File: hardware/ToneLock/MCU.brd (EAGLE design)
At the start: 160 x 100 mm, 13 parts, among them U1 LD1117S33TR, U2 MP45DT02, U3 LIS3DSHTR

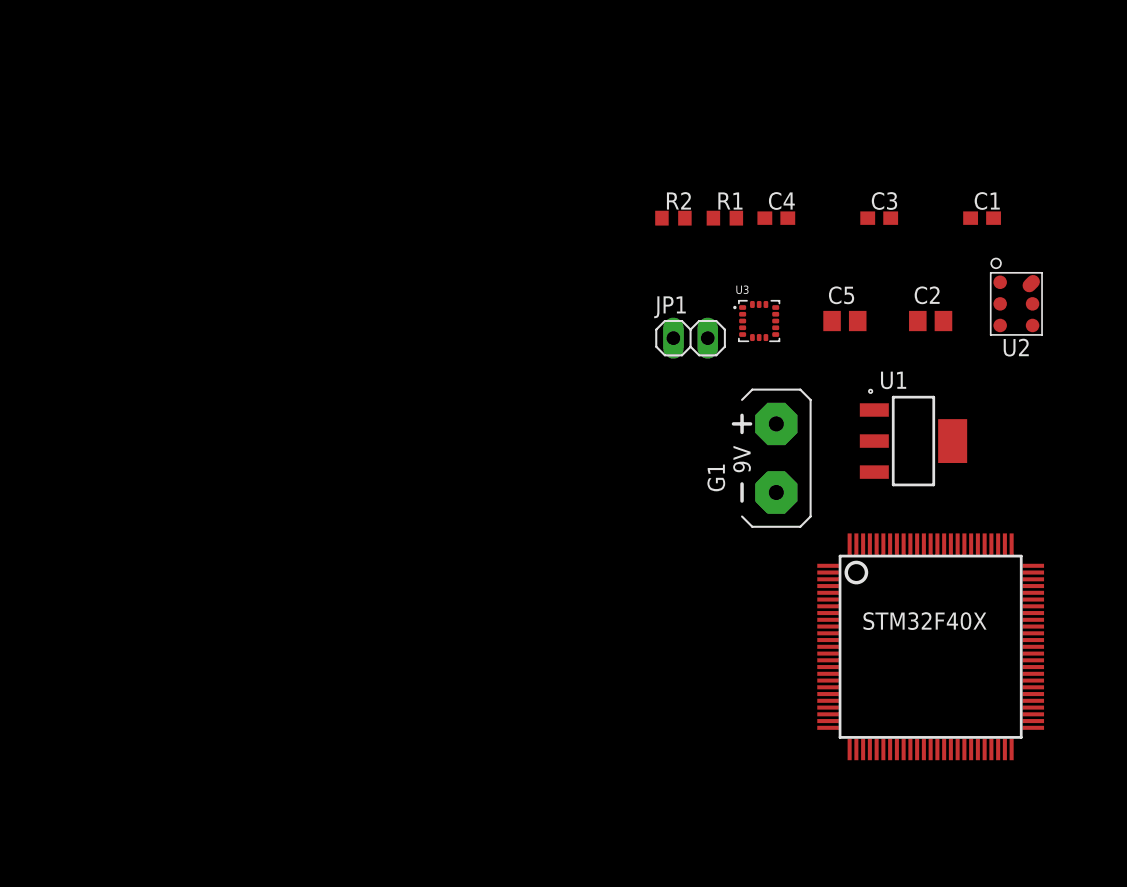
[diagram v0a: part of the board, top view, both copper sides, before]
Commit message: Changed VCC header
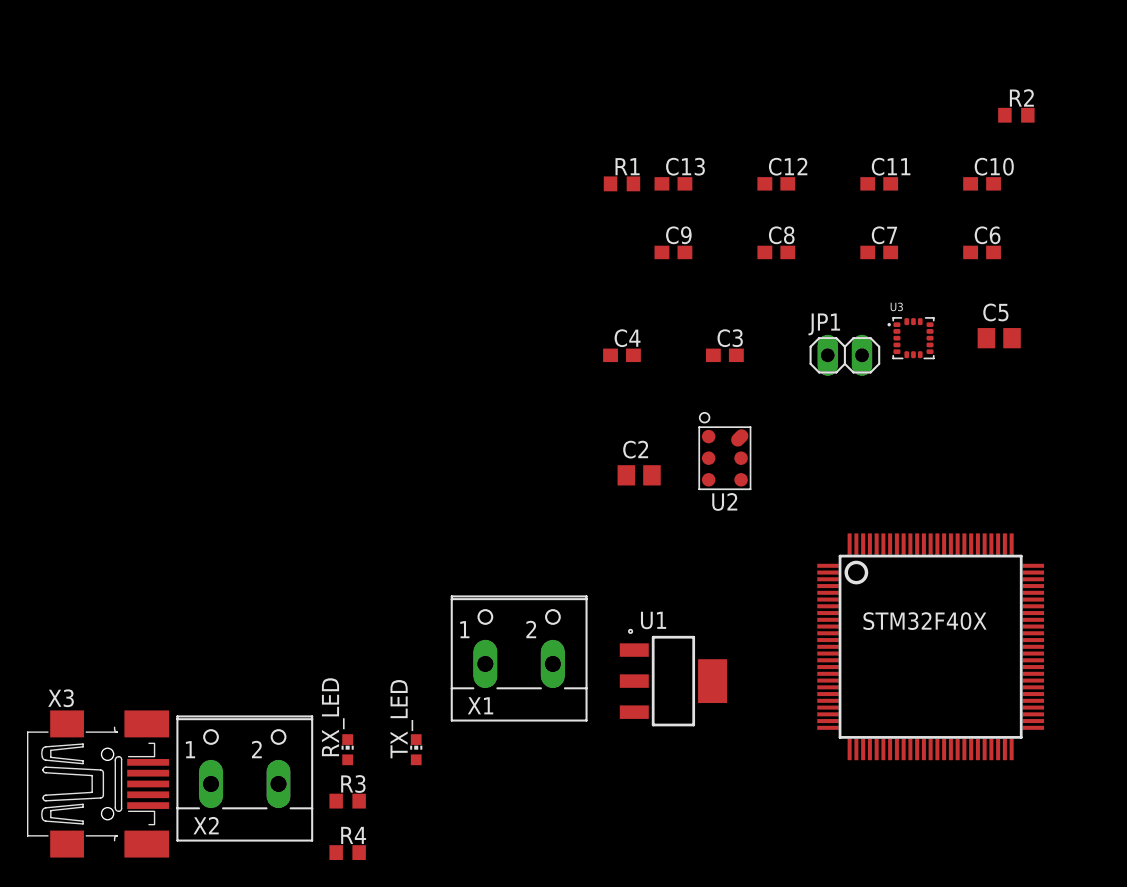
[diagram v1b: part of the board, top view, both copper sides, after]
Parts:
- removed C1: 100nF, resistor:C0603
- removed G1: AB9V, battery:AB9V
- added C10, C11, C12, C13, C6, C7, C8, C9: 100nF, resistor:C0603
- added R3, R4: 330, resistor:R0603
- added RX_LED, TX_LED: (no value), led:CHIP-LED0603
- added X1, X2: (no value), con-wago-500:W237-102
- added X3: MINI-USB-32005-201, con-cypressindustries:32005-201
- moved R2 26.5 mm to (-15.2, 48.3)
- moved U1 25.1 mm to (-40.6, 6.35)
- moved C2 24.4 mm to (-43.2, 21.6)
- moved U2 24.4 mm to (-36.8, 22.9)
- moved C3 15.3 mm to (-36.8, 30.5)
- moved C4 15.3 mm to (-44.5, 30.5)
- moved C5 11.5 mm to (-16.5, 31.8)
- moved U3 11.5 mm to (-22.9, 31.8)
- moved JP1 11.5 mm to (-27.9, 30.5)
- moved R1 8.03 mm to (-44.5, 43.2)
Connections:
- removed net N$2: G1.+, U1.3
- new net N$4: R4.1, RX_LED.C
- new net VCC: U1.3, X1.2
- net GND: now also C10.2, C11.2, C12.2, C13.2, C6.2, C7.2, C8.2, C9.2, U$1.10, U$1.20, U$1.27, U$1.74, U$1.99, X1.1; no longer C1.1, G1.-, U3.13, U3.15, U3.16
- net N$1: now also R3.1, TX_LED.C; no longer C1.2, U$1.11, U$1.6
- net USART2_RX: now also R4.2
- net USART2_TX: now also R3.2
- net VDD: now also C10.1, C11.1, C12.1, C13.1, C6.1, C7.1, C8.1, C9.1, RX_LED.A, TX_LED.A, U$1.100, U$1.11, U$1.19, U$1.21, U$1.22, U$1.28, U$1.50, U$1.6, U$1.75

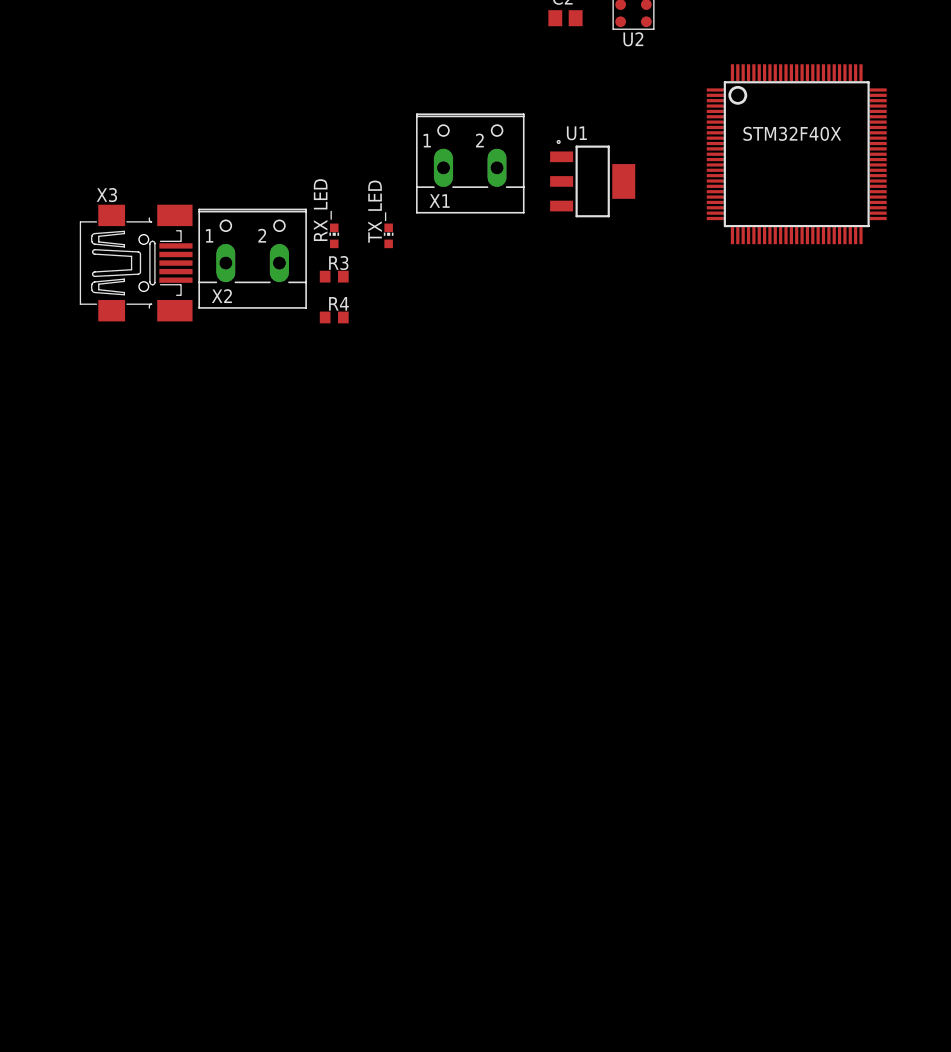
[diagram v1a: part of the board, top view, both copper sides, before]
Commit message: Added BOOT0 and NRST setups, power LED, Debugger
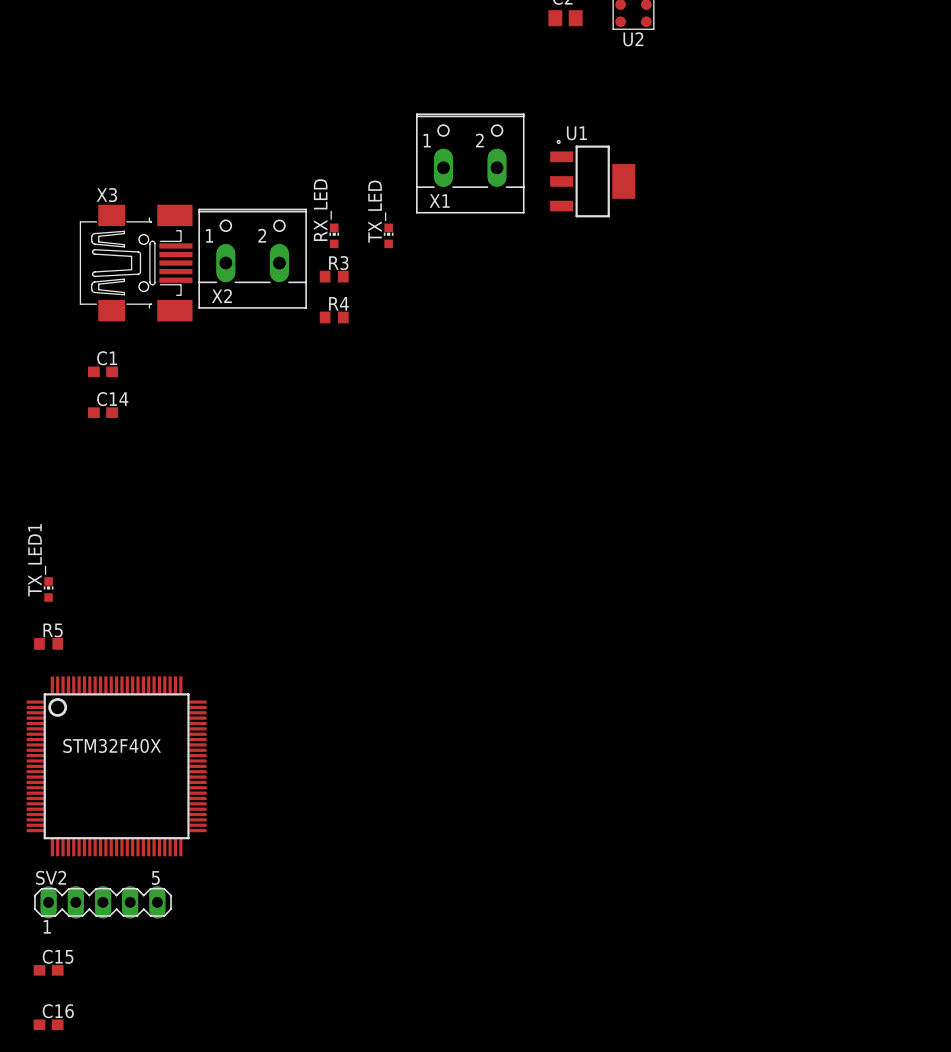
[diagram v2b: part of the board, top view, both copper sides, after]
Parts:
- added C1, C14: 2.2uF, resistor:C0603
- added C15, C16: 10uF, resistor:C0603
- added R5: 330, resistor:R0603
- added SV2: (no value), con-lstb:MA05-1
- added TX_LED1: (no value), led:CHIP-LED0603
- U$1: value STM32F40XSTM32D40X -> STM32F407STM32D40X
- moved U$1 85.4 mm to (-85.1, -48.3)
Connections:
- removed net VCC: U1.3, X1.2
- new net +12V: X1.2
- new net +5V: X3.1
- new net N$2: C14.1, U$1.73
- new net N$5: C1.1, U$1.49
- new net N$6: U1.3
- new net N$7: R5.1, TX_LED1.C
- new net NRST: SV2.5, U$1.14
- new net SWCLK: SV2.2, U$1.76
- new net SWDIO: SV2.4, U$1.72
- net GND: now also C1.2, C14.2, C15.2, C16.2, R5.2, SV2.3, U$1.94, X2.2, X3.5
- net VDD: now also C15.1, C16.1, SV2.1, TX_LED1.A

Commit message: Completed schematic
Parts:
- added D1, D2: BAT54C, diode:SOT23
- added DBG_LED1, DBG_LED2, DBG_LED3, DBG_LED4: (no value), led:CHIP-LED0603
- added Q1: IRLML6346, bss138_10:SOT23
- added R11, R6, R7, R8: 330, resistor:R0603
- added R9: 10k, resistor:R0603
- moved R2 238.6 mm to (-119.4, -166.4)
- moved R1 217.8 mm to (-119.4, -161.3)
- moved R4 140.6 mm to (-119.4, -135.9)
- moved R3 139.4 mm to (-119.4, -130.8)
- moved R5 107.8 mm to (-119.4, -141.0)
- renumbered TX_LED1 to POWER_LED
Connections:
- new net DBG_LED1: DBG_LED1.A, U$1.59
- new net DBG_LED2: DBG_LED2.A, U$1.60
- new net DBG_LED3: DBG_LED3.A, U$1.61
- new net DBG_LED4: DBG_LED4.A, U$1.62
- new net MOSFET_GATE: Q1.1, R9.2, U$1.1
- new net N$10: DBG_LED3.C, R6.1
- new net N$11: DBG_LED2.C, R7.1
- new net N$12: DBG_LED1.C, R8.1
- new net N$8: D2.3, Q1.2, X2.1
- new net N$9: DBG_LED4.C, R5.1
- net +12V: now also D1.2, Q1.3
- net +5V: now also D1.1
- net GND: now also D2.1, D2.2, R1.1, R11.2, R6.2, R7.2, R8.2, R9.1; no longer R2.1
- net N$1: now also POWER_LED.C, R11.1; no longer R3.1, TX_LED.C
- net N$3: now also R1.2, R2.1; no longer R1.1, R2.2
- net N$4: now also R3.1; no longer R4.1
- net N$6: now also D1.3
- net N$7: now also R4.1, TX_LED.C; no longer POWER_LED.C, R5.1
- net USART2_RX: now also R3.2; no longer R4.2
- net USART2_TX: now also R4.2; no longer R3.2
- net VDD: now also R2.2; no longer R1.2

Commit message: Fixed MOSFET switch, grouped all components
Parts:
- added C17: 100nF, resistor:C0603
- moved R2 205.1 mm to (-40.5, 23.0), turned to 90 degrees
- moved R1 196.8 mm to (-40.5, 19.0), turned to 90 degrees
- moved R8 157.0 mm to (-26.0, -30.0), turned to 180 degrees
- moved R7 155.3 mm to (-26.0, -27.0), turned to 180 degrees
- moved R6 153.7 mm to (-26.0, -24.0), turned to 180 degrees
- moved R5 152.0 mm to (-26.0, -21.0), turned to 180 degrees
- moved Q1 135.1 mm to (-108.0, -37.5), turned to 90 degrees
- moved R9 134.7 mm to (-105.0, -37.5), turned to 270 degrees
- moved DBG_LED4 115.7 mm to (-23.0, -21.0), turned to 90 degrees
- moved DBG_LED3 109.9 mm to (-23.0, -24.0), turned to 90 degrees
- moved R4 109.0 mm to (-68.5, -39.5), turned to 270 degrees
- moved DBG_LED2 104.0 mm to (-23.0, -27.0), turned to 90 degrees
- moved U3 103.5 mm to (-35.0, -71.0)
- moved R3 102.4 mm to (-73.0, -39.5), turned to 270 degrees
- moved C4 100.0 mm to (-30.5, -68.5)
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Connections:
- removed net N$8: D2.3, Q1.2, X2.1
- new net N$13: D2.2, Q1.3, X2.2
- net +12V: now also D2.3, X2.1; no longer Q1.3
- net GND: now also C17.2, Q1.2; no longer D2.2, X2.2
- net VDD: now also C17.1
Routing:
- net N$3: track 0.00 -> 6.75 mm
- net N$9: track 0.00 -> 1.40 mm
- net N$12: track 0.00 -> 1.40 mm
- net N$11: track 0.00 -> 1.40 mm
- net N$10: track 0.00 -> 1.40 mm
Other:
- board size 160 x 100 mm -> 71 x 56.5 mm

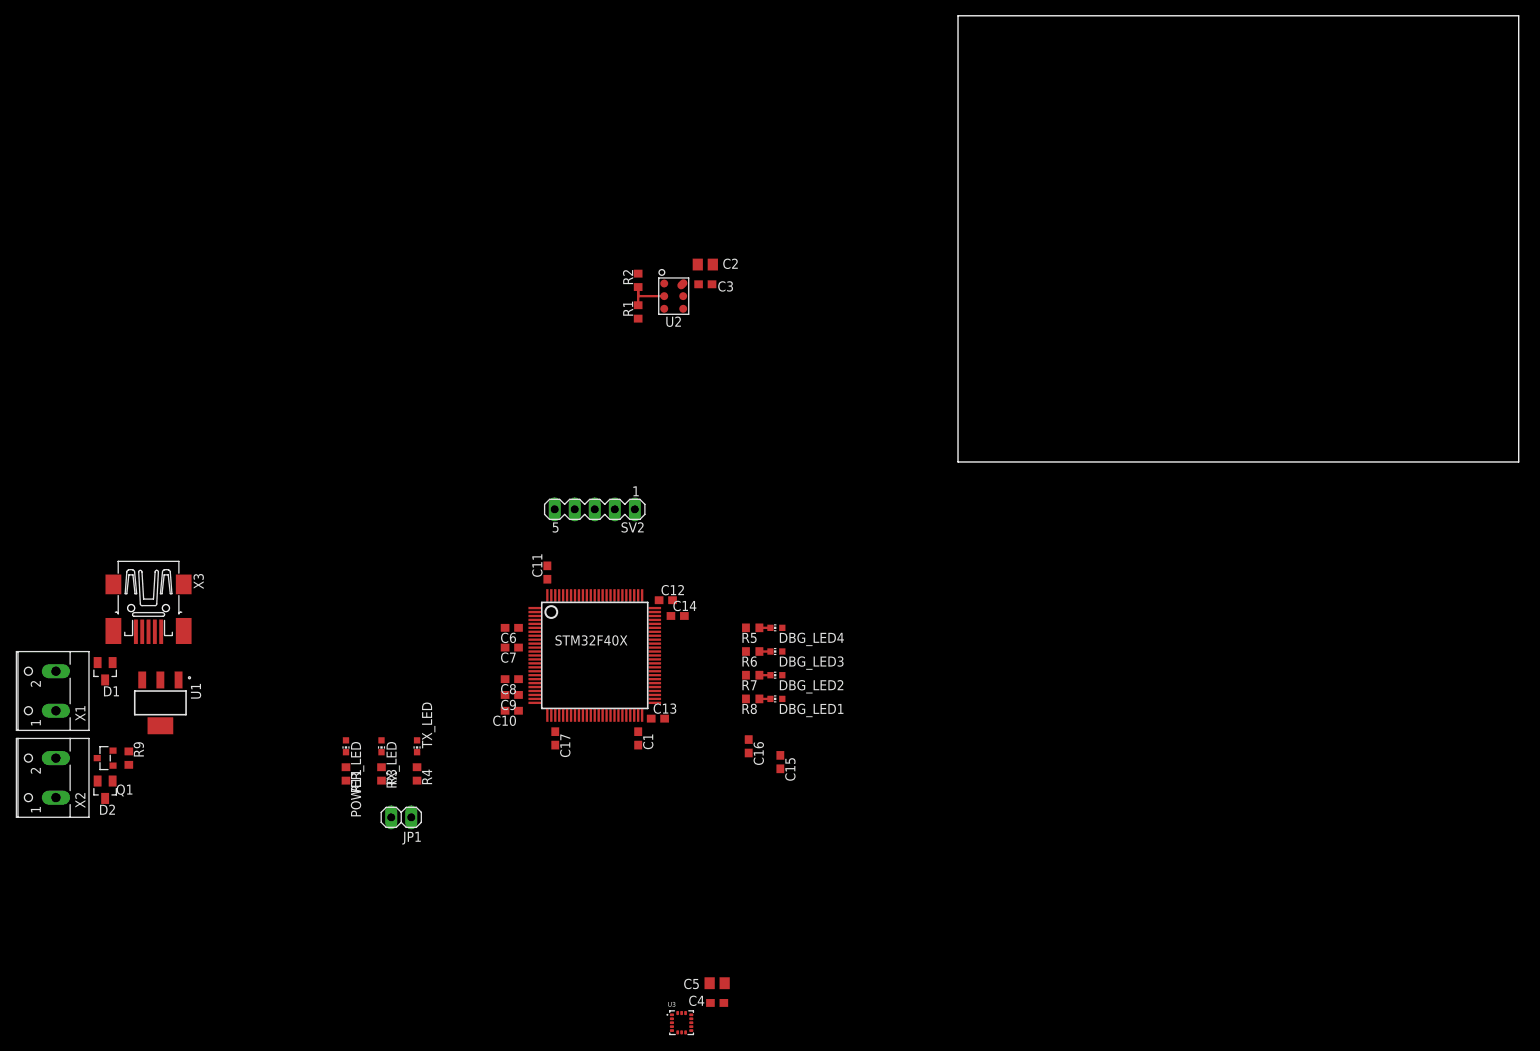
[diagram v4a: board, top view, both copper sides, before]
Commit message: All VCC and signals routed, GND TODO
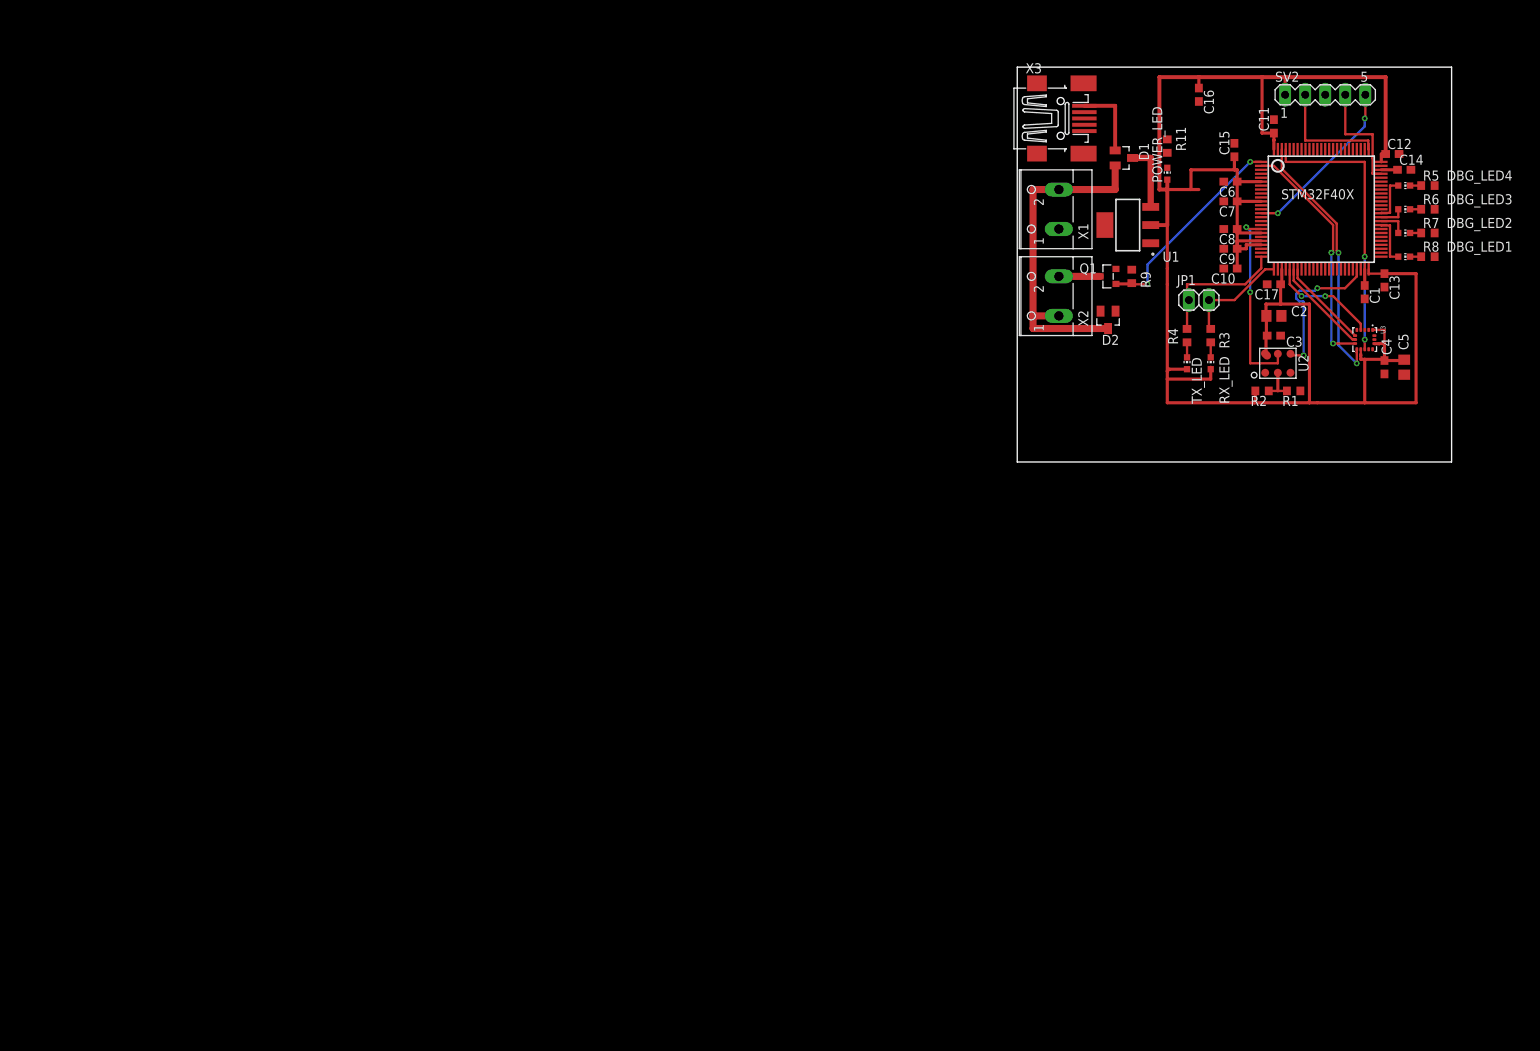
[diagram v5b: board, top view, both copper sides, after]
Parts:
- moved D1 144.5 mm to (21.0, 38.5), turned to 270 degrees
- moved Q1 140.9 mm to (19.0, 23.5)
- moved R9 140.9 mm to (22.0, 23.5)
- moved X1 140.9 mm to (11.5, 32.0)
- moved X2 140.9 mm to (11.5, 21.0)
- moved D2 140.2 mm to (19.0, 18.0)
- moved U1 136.6 mm to (21.5, 30.0), turned to 180 degrees
- moved X3 131.1 mm to (13.0, 43.5), turned to 0 degrees
- moved R11 130.9 mm to (26.5, 40.0), turned to 90 degrees
- moved POWER_LED 126.8 mm to (26.5, 36.5), turned to 0 degrees
- moved U3 122.3 mm to (51.5, 15.5), turned to 270 degrees
- moved JP1 120.4 mm to (30.5, 20.5)
- moved R3 118.8 mm to (32.0, 16.0), turned to 90 degrees
- moved C5 116.8 mm to (56.5, 12.0), turned to 270 degrees
- moved C4 116.7 mm to (54.0, 12.0), turned to 270 degrees
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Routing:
- net VDD: track 0.20 -> 257.6 mm
- net +12V: track 0.10 -> 43.8 mm
- net MEMS_INT1: track 0.00 -> 35.3 mm, vias 0 -> 2
- net MEMS_INT2: track 0.00 -> 32.8 mm, vias 0 -> 2
- net MEMS_CS: track 0.00 -> 30.3 mm, vias 0 -> 2
- net MOSFET_GATE: track 0.00 -> 26.4 mm, vias 0 -> 2
- net MIC_PDM: track 0.00 -> 24.1 mm, vias 0 -> 2
- net NRST: track 0.00 -> 21.7 mm, vias 0 -> 2
- net MIC_CLK: track 0.00 -> 19.7 mm, vias 0 -> 2
- net USART2_TX: track 0.00 -> 17.7 mm
- net SWCLK: track 0.00 -> 14.9 mm
- net SWDIO: track 0.00 -> 14.6 mm
- net MEMS_SCK: track 0.00 -> 13.7 mm, vias 0 -> 2
- net USART2_RX: track 0.00 -> 13.6 mm
- net MEMS_MISO: track 0.00 -> 12.3 mm
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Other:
- board size 71 x 56.5 mm -> 55 x 50 mm
